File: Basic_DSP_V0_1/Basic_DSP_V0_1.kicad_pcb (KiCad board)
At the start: 6 copper layers, 60 x 100 mm, 175 parts, among them J1 53048-0310, J10 53048-0310, J11 53048-0410, J12 Conn_ARM_SWD_TagConnect_TC2030, J13 USB_C_Receptacle, J14 53048-0210, J15 53048-0210, J16 Conn_02x08_Odd_Even, J2 53048-0310, J3 53048-0310, J6 53048-0410, J7 53048-0310, J8 53048-0310, J9 53048-0310, Q1 AO3400A, Q2 AO3400A, Q3 AO3400A, U1 STM32F415RGTx, U10 TLV9161IDBVR, U2 CS4270, U3 TLV76733QWDRBRQ1, U5 NCP718BSN500T1G, U6 TLV9161IDBVR, U7 TLV9161IDBVR, U8 TLV9161IDBVR, U9 TLV9161IDBVR, Y1 ABM8G-24.000MHZ-18-D2Y-T3

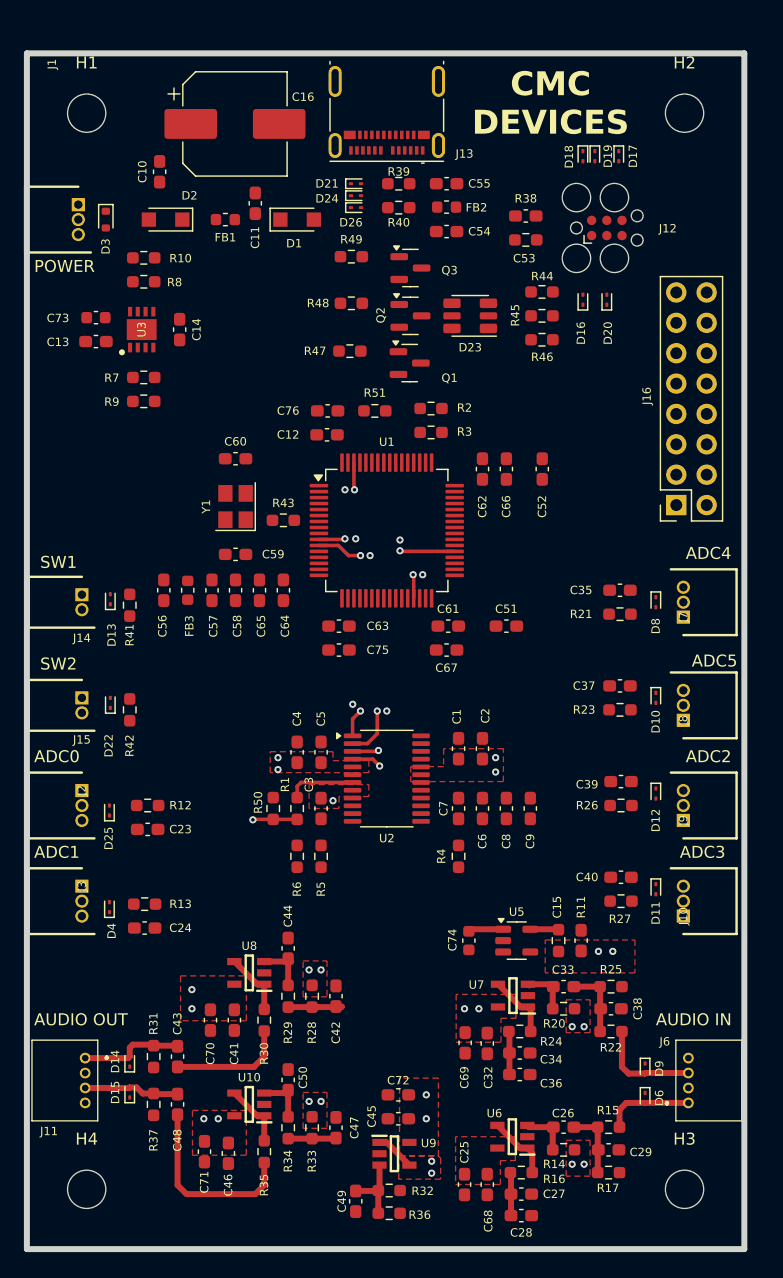
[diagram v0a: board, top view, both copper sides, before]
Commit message: More layout on Basic_DSP_V0_1 and a change of USB connector
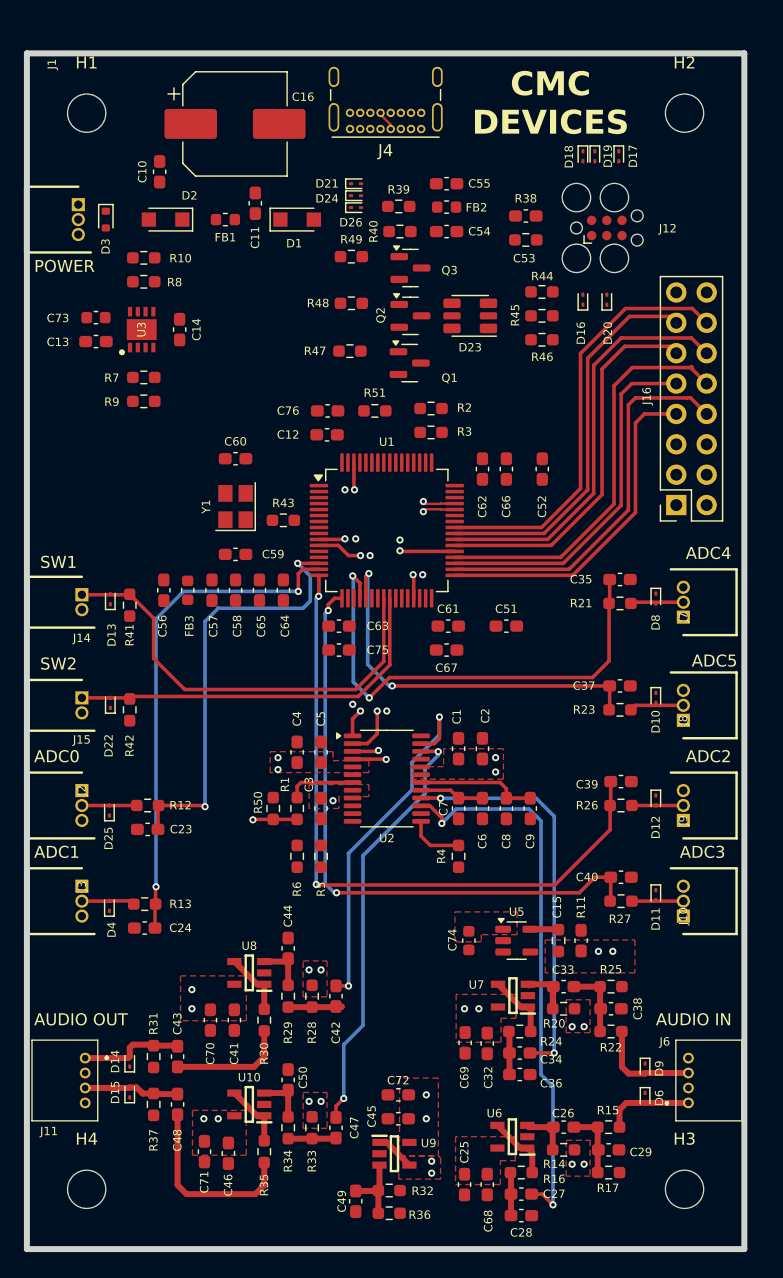
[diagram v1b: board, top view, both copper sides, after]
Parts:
- removed J13: USB_C_Receptacle, Connector_USB:USB_C_Receptacle_Molex_105450-0101
- added J4: USB_C_Receptacle_USB2.0_16P, Connector_USB:USB_C_Receptacle_GCT_USB4085, F.Cu at (106.4, 310.4)
- moved R40 2.00 mm to (104.6, 319.0)
- moved R39 1.90 mm to (104.5, 316.9)
- moved C35 0.90 mm to (123.0, 348.1)
- moved R21 0.90 mm to (123.0, 350.1)
- moved D12 0.58 mm to (126.0, 366.6)
- moved D11 0.50 mm to (126.0, 374.5)
- moved D8 0.30 mm to (126.0, 349.7)
- moved D4 0.10 mm to (80.3, 375.4)
- turned C23 to 180 degrees
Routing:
- net /Connections/ADC_IN2: track 0.00 -> 56.5 mm, vias 0 -> 2
- net /Connections/ADC_IN3: track 0.00 -> 51.6 mm, vias 0 -> 2
- net /Analogue/CODEC_IN_L: track 0.00 -> 46.5 mm, vias 0 -> 2
- net /Connections/ADC_IN1: track 0.00 -> 42.1 mm, vias 0 -> 2
- net /Connections/ADC_IN4: track 0.00 -> 41.1 mm, vias 0 -> 2
- net /Connections/USB_D-: track 0.00 -> 39.0 mm, vias 0 -> 1
- net /Connections/USB_D+: track 0.00 -> 38.3 mm, vias 0 -> 1
- net /Connections/SWITCH_0: track 0.00 -> 36.8 mm
- net /Connections/ADC_IN0: track 0.00 -> 36.3 mm, vias 0 -> 2
- net /Connections/GPIO11: track 0.00 -> 35.8 mm
- net /Analogue/CODEC_OUT_L: track 0.00 -> 35.6 mm, vias 0 -> 2
- net /Connections/GPIO9: track 0.00 -> 34.9 mm
- net /Connections/GPIO7: track 0.00 -> 34.2 mm
- net /Analogue/CODEC_IN_R: track 0.00 -> 33.7 mm, vias 0 -> 2
- net /Connections/ADC_IN5: track 0.00 -> 32.8 mm, vias 0 -> 2
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- added copper zone on In3.Cu, net +5VA
- added copper zone on In3.Cu, net +VREF
- added copper zone on F.Cu, net Net-(D1-K)
- removed copper zone on In2.Cu, net +5VA
- removed copper zone on In2.Cu, net +VREF

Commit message: More layout work
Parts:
- moved R2 37.5 mm to (109.5, 371.2), turned to -90 degrees
- moved R3 35.7 mm to (111.5, 371.2), turned to -90 degrees
- moved R49 9.50 mm to (97.5, 330.1), turned to -90 degrees
- moved R39 6.60 mm to (98.9, 313.4), turned to 90 degrees
- moved C55 5.38 mm to (104.6, 318.7), turned to 0 degrees
- moved D26 5.23 mm to (103.9, 312.7), turned to 90 degrees
- moved R48 5.19 mm to (99.6, 330.1), turned to -90 degrees
- moved R4 4.10 mm to (113.6, 371.2)
- moved C54 4.04 mm to (109.1, 315.0)
- moved R40 4.00 mm to (104.6, 315.0)
- moved D24 3.85 mm to (102.9, 312.7), turned to 90 degrees
- moved FB2 3.73 mm to (104.8, 316.9), turned to 180 degrees
- moved D21 2.31 mm to (101.1, 312.7), turned to 90 degrees
- moved R51 2.00 mm to (102.5, 336.0)
- moved R47 1.69 mm to (101.7, 330.1), turned to -90 degrees
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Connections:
- C55 pad 1: Net-(C55-Pad1) -> VBUS_FILT
- FB2 pad 2: Net-(C55-Pad1) -> VBUS_FILT
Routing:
- net /Power/V_ENABLE: track 0.00 -> 86.4 mm, vias 0 -> 3
- net /CODEC/I2C1_SCL: track 0.00 -> 48.4 mm, vias 0 -> 2
- net /CODEC/I2C1_SDA: track 0.00 -> 42.1 mm, vias 0 -> 2
- net /Connections/GPIO1: track 0.00 -> 41.5 mm
- net /Connections/GPIO0: track 0.00 -> 38.9 mm
- net /Connections/GPIO3: track 0.00 -> 30.7 mm, vias 0 -> 1
- net /Connections/GPIO2: track 0.00 -> 29.6 mm, vias 0 -> 1
- net Net-(Q3-G): track 0.00 -> 14.3 mm
- net /Processor/LED_GREEN: track 0.00 -> 13.6 mm
- net Net-(U2-AD0/~{CS}/I2S/~{LJ}): track 0.00 -> 13.6 mm
- net /Processor/LED_RED: track 0.00 -> 11.8 mm
- net /Processor/MCU_CKL_IN: track 0.00 -> 11.0 mm
- net /Processor/LED_BLUE: track 0.00 -> 10.5 mm
- net Net-(J4-CC2): track 0.00 -> 10.3 mm
- net Net-(Q2-G): track 0.00 -> 8.36 mm
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
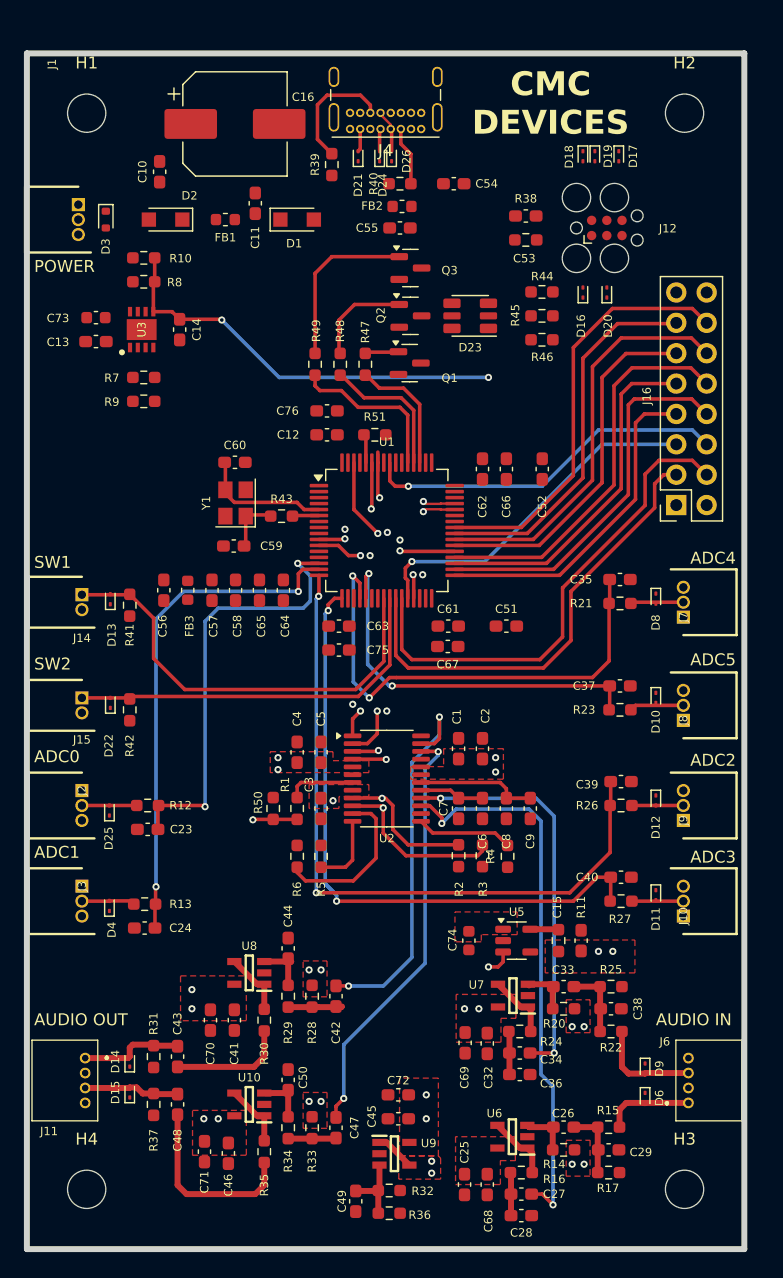
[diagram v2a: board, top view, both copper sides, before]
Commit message: More layout updates
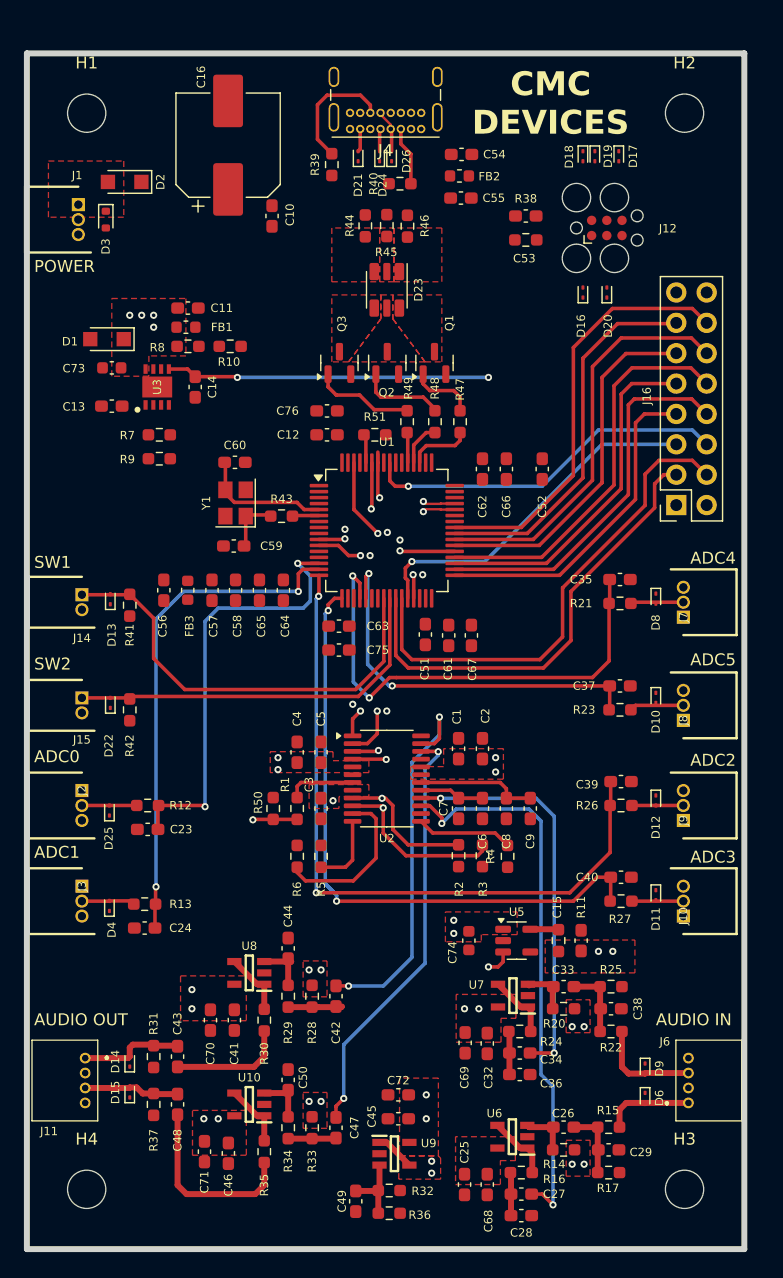
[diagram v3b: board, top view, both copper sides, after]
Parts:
- moved D1 18.8 mm to (80.1, 328.0), turned to 180 degrees
- moved R44 15.8 mm to (101.7, 318.5), turned to 90 degrees
- moved R45 15.0 mm to (103.5, 318.5), turned to 90 degrees
- moved R46 14.7 mm to (105.2, 318.6), turned to 90 degrees
- moved C11 10.4 mm to (86.9, 325.4), turned to 0 degrees
- moved R10 10.3 mm to (90.4, 328.6), turned to 0 degrees
- moved C10 10.1 mm to (93.9, 317.7)
- moved Q3 9.91 mm to (99.5, 330.0), turned to 90 degrees
- moved FB1 9.59 mm to (86.7, 327.0), turned to 180 degrees
- moved R48 9.27 mm to (107.5, 334.9)
- moved R47 9.27 mm to (109.6, 334.9)
- moved R49 9.07 mm to (105.2, 334.9)
- moved D23 7.31 mm to (103.5, 323.9), turned to -90 degrees
- moved C51 6.81 mm to (106.7, 352.7), turned to -90 degrees
- moved R8 6.54 mm to (86.9, 328.6)
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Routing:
- net /Processor/LED_GREEN: track 13.6 -> 2.58 mm
- net /Processor/LED_RED: track 11.8 -> 3.89 mm
- net /Power/V_ENABLE: track 86.4 -> 78.6 mm
- net Net-(Q3-G): track 14.3 -> 8.79 mm
- net /Processor/LED_BLUE: track 10.5 -> 5.32 mm
- net Net-(Q1-G): track 2.79 -> 5.57 mm
- net Net-(Q2-G): track 8.36 -> 7.26 mm
- net Net-(D1-K): vias 0 -> 6
- added copper zone on In3.Cu, net Net-(D1-K)
- added copper zone on F.Cu, net Net-(D23-BA)
- added copper zone on F.Cu, net Net-(D23-BK)
- added copper zone on F.Cu, net Net-(D23-GA)
- added copper zone on F.Cu, net Net-(D23-GK)
- added copper zone on F.Cu, net Net-(D23-RA)
- added copper zone on F.Cu, net Net-(D23-RK)
- added copper zone on F.Cu, net VCC

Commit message: Minor layout work
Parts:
- removed C64: 100n, Capacitor_SMD:C_0603_1608Metric_Pad1.08x0.95mm_HandSolder
- moved C56 1.55 mm to (86.4, 349.0), turned to 90 degrees
- moved C57 1.55 mm to (90.4, 349.0), turned to -90 degrees
- moved C58 1.55 mm to (92.4, 349.0), turned to -90 degrees
- moved C65 1.55 mm to (94.4, 349.0)
- moved FB3 1.55 mm to (88.4, 349.0), turned to 90 degrees
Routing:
- net /CODEC/CODEC_~{RST}: track 0.00 -> 23.7 mm, vias 0 -> 2
- net +3V3_FILT: track 0.00 -> 6.03 mm
- net /Connections/ADC_IN0: track 36.3 -> 39.5 mm
- net /CODEC/I2S_BCLK: track 21.2 -> 22.0 mm
- added copper zone on F.Cu, net +3V3_FILT
- added copper zone on F.Cu, net Net-(U1-VCAP_1)

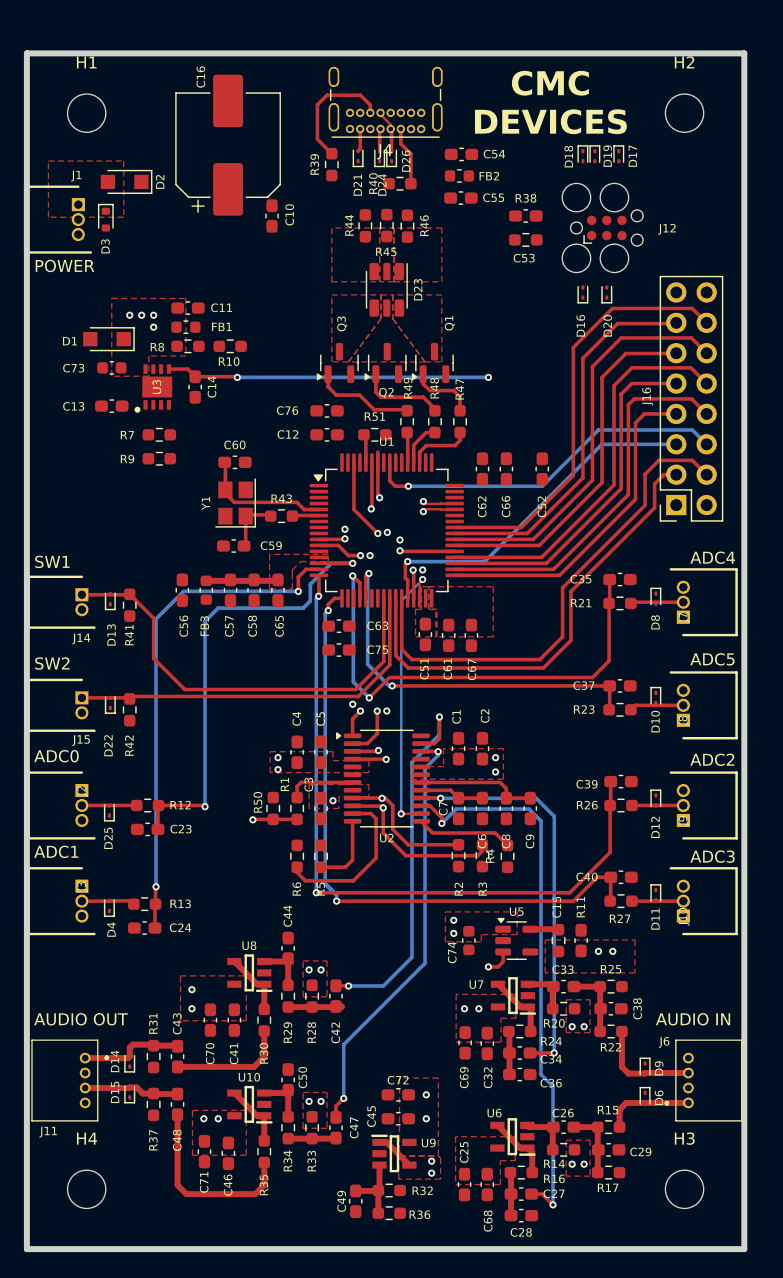
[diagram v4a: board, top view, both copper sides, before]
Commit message: Layout and removal of PDN ferrites
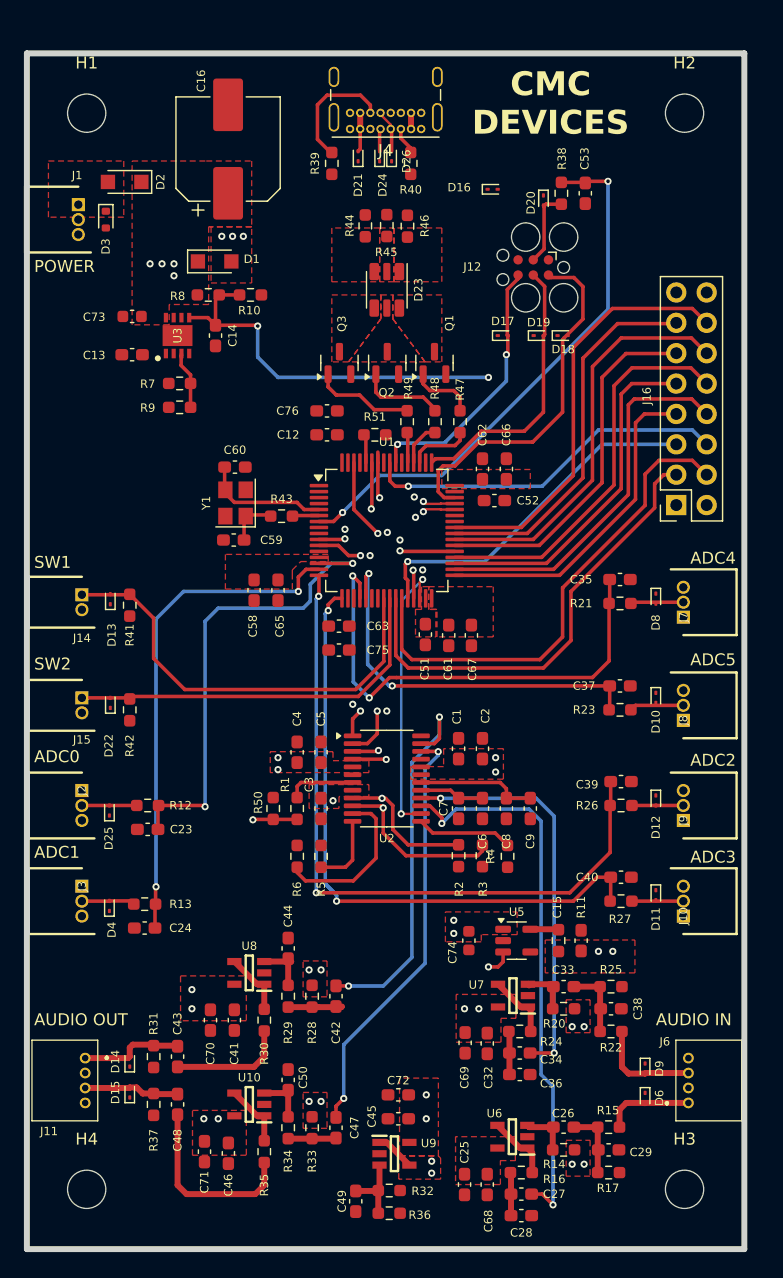
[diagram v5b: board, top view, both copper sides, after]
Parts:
- removed C10, C11: 2u2, Capacitor_SMD:C_0603_1608Metric_Pad1.08x0.95mm_HandSolder
- removed C54, C55, C56, C57: 100n, Capacitor_SMD:C_0603_1608Metric_Pad1.08x0.95mm_HandSolder
- removed FB1, FB2, FB3: 120R, Inductor_SMD:L_0603_1608Metric
- R11: value 10R -> 0R
- moved D17 17.9 mm to (113.2, 327.7), turned to 0 degrees
- moved D19 15.7 mm to (116.2, 327.7), turned to 0 degrees
- moved D18 15.1 mm to (118.2, 327.7), turned to 0 degrees
- moved D16 11.5 mm to (112.3, 315.5), turned to 0 degrees
- moved D1 11.1 mm to (89.1, 321.5), turned to 0 degrees
- moved D20 9.35 mm to (116.6, 316.4), turned to -90 degrees
- moved J12 6.98 mm to (115.8, 322.0), turned to 180 degrees
- moved C53 5.33 mm to (120.1, 315.8), turned to -90 degrees
- moved R38 4.91 mm to (118.1, 315.8), turned to 90 degrees
- moved C52 4.79 mm to (112.5, 341.5), turned to 0 degrees
- moved C13 4.62 mm to (82.2, 329.3)
- moved C14 4.62 mm to (89.2, 327.7)
- moved R7 4.62 mm to (86.2, 331.7)
- moved R9 4.62 mm to (86.2, 333.7)
- moved U3 4.62 mm to (86.0, 327.7)
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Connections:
- C16 pad 1: Net-(D2-K) -> Net-(D1-K)
- C58 pad 1: +3V3_FILT -> +3V3
- C65 pad 1: +3V3_FILT -> +3V3
- D1 pad 2: VBUS_FILT -> VBUS
- D2 pad 1: Net-(D2-K) -> Net-(D1-K)
- J4 pad S1: unconnected-(J4-SHIELD-PadS1) -> GND
- U1 pad 13: +3V3_FILT -> +3V3
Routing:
- net /Processor/MCU_~{RST}: track 0.00 -> 46.2 mm, vias 0 -> 2
- net /Processor/SWDIO: track 0.00 -> 30.2 mm
- net /Processor/SWCLK: track 0.00 -> 23.0 mm
- net /Processor/SWO: track 0.00 -> 22.2 mm, vias 0 -> 2
- net /Processor/nRESET: track 0.00 -> 6.45 mm
- net +3V3_FILT: track 6.03 -> 0.00 mm
- net /Power/V_ENABLE: track 78.6 -> 84.6 mm
- net Net-(U3-SNS): track 0.00 -> 4.84 mm
- net VBUS: track 1.93 -> 4.63 mm, vias 0 -> 3
- net Net-(J4-CC1): track 5.06 -> 2.45 mm
- net GND: vias 7 -> 9
- added copper zone on F.Cu, net VBUS
- added copper zone on In3.Cu, net VBUS
- removed copper zone on F.Cu, net +3V3_FILT
